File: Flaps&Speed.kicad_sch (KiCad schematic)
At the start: 12 parts, among them J1 CAN-In, J2 CAN-Out, J3 Conn_01x08_Pin, J4 Conn_01x04_Pin, U1 SN65HVD230

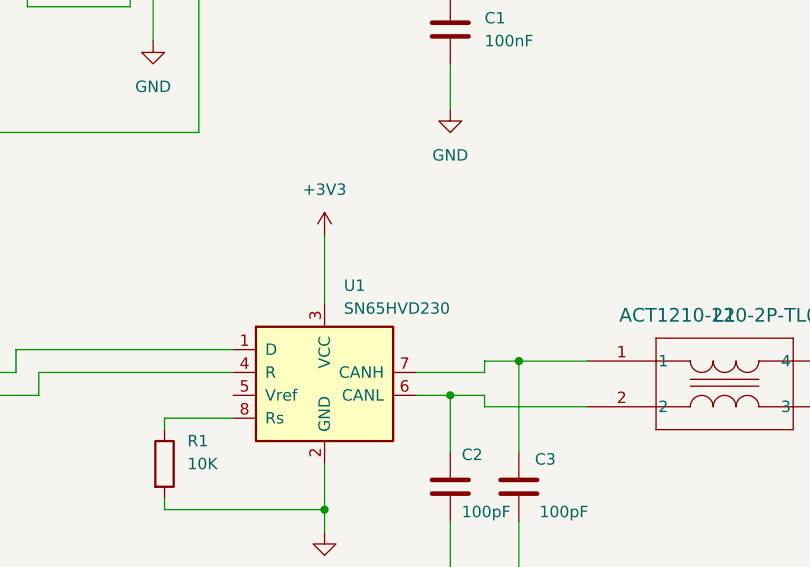
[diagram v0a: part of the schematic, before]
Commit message: Adjust BOM settings and properties in KiCad project: updated field orders, added new properties, and fixed naming errors (e.g., "Flaps&Spedd" to "Flaps&Speed").
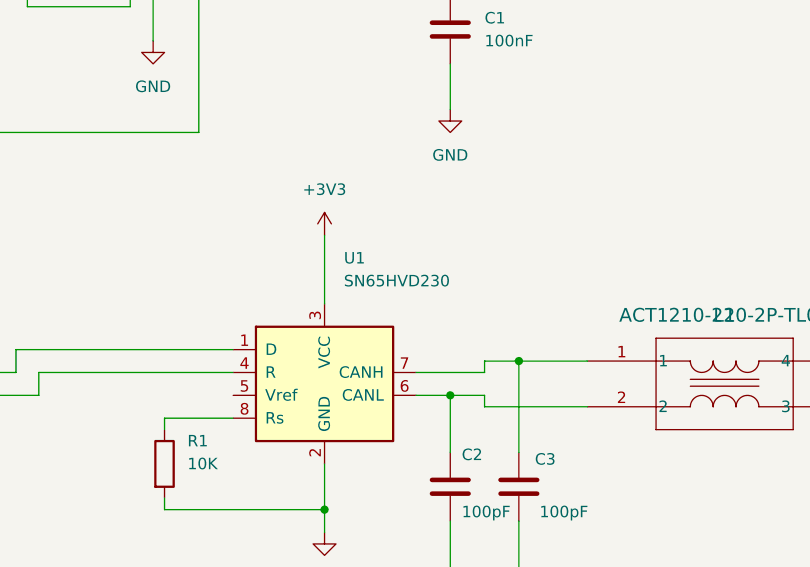
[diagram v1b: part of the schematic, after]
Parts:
- C1: MPN (none) -> GRM31CR71H104KA01L; Manufacturer (none) -> Murata; Qty (none) -> 1; Type (none) -> smd
- C2, C3: MPN (none) -> GRM31C5C1H101JA01L; Manufacturer (none) -> Murata; Qty (none) -> 1; Type (none) -> smd
- J3, J4: now left out of the parts list
- L1: MPN (none) -> ACT1210-220-2P-TL00; Manufacturer (none) -> TDK; Qty (none) -> 1; Type (none) -> smd
- R1: MPN (none) -> RC1206FR-0710KL; Manufacturer (none) -> Yageo; Qty (none) -> 1; Type (none) -> smd
- R2: MPN (none) -> RC1206FR-07120RL; Manufacturer (none) -> Yageo; Qty (none) -> 1; Type (none) -> smd
- U1: MPN (none) -> SN65HVD230DR; Manufacturer (none) -> Texas Instruments; Qty (none) -> 1; Type (none) -> smd
